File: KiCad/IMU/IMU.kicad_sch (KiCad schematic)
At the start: 10 parts, among them J1 Conn_02x20_Odd_Even

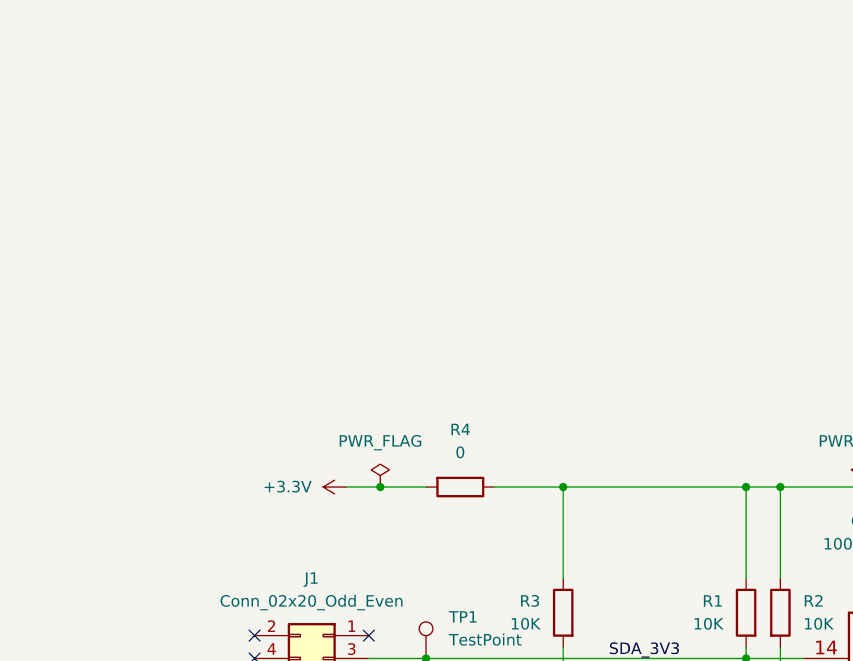
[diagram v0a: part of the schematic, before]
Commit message: Add buck 3V3 converter
Add buck 3V3 converter
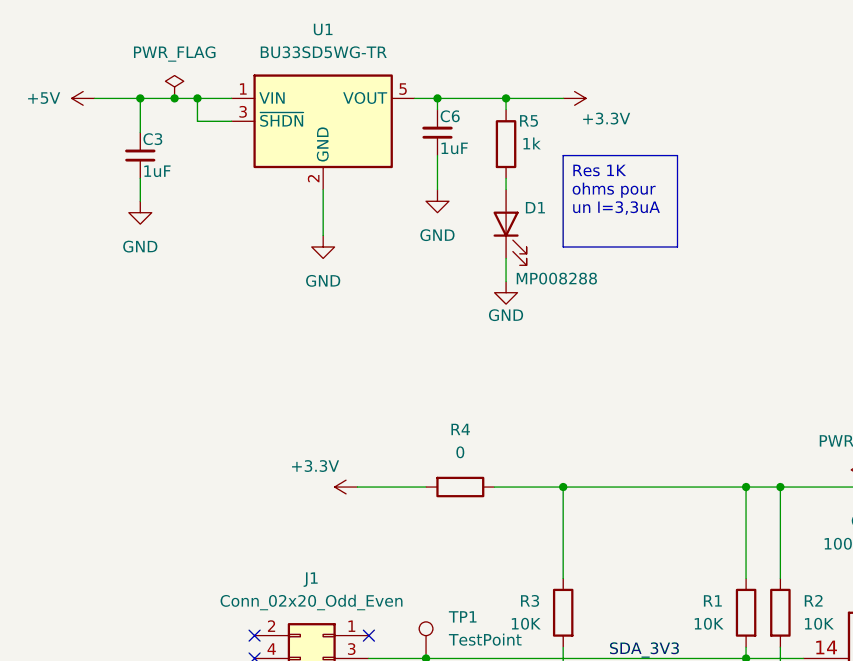
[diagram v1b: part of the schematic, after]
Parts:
- added C3, C6: 1uF, Capacitor_SMD:C_0603_1608Metric_Pad1.08x0.95mm_HandSolder, symbol Device:C_Small
- added D1: MP008288, LED_SMD:LED_0603_1608Metric, symbol Device:LED
- added R5: 1k, Resistor_SMD:R_0603_1608Metric_Pad0.98x0.95mm_HandSolder, symbol Device:R
- added U1: BU33SD5WG-TR, Package_TO_SOT_SMD:SOT-23-5, symbol Regulator_Linear:MCP1802x-xx02xOT
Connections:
- net +3.3V: now also C6.2, R5.1, U1.5 (VOUT)
- net GND: now also C3.1, C6.1, D1.1 (K), U1.2 (GND)
- new net: D1.2 (A), R5.2
- new net +5V: C3.2, U1.1 (VIN), U1.3 (~{SHDN})

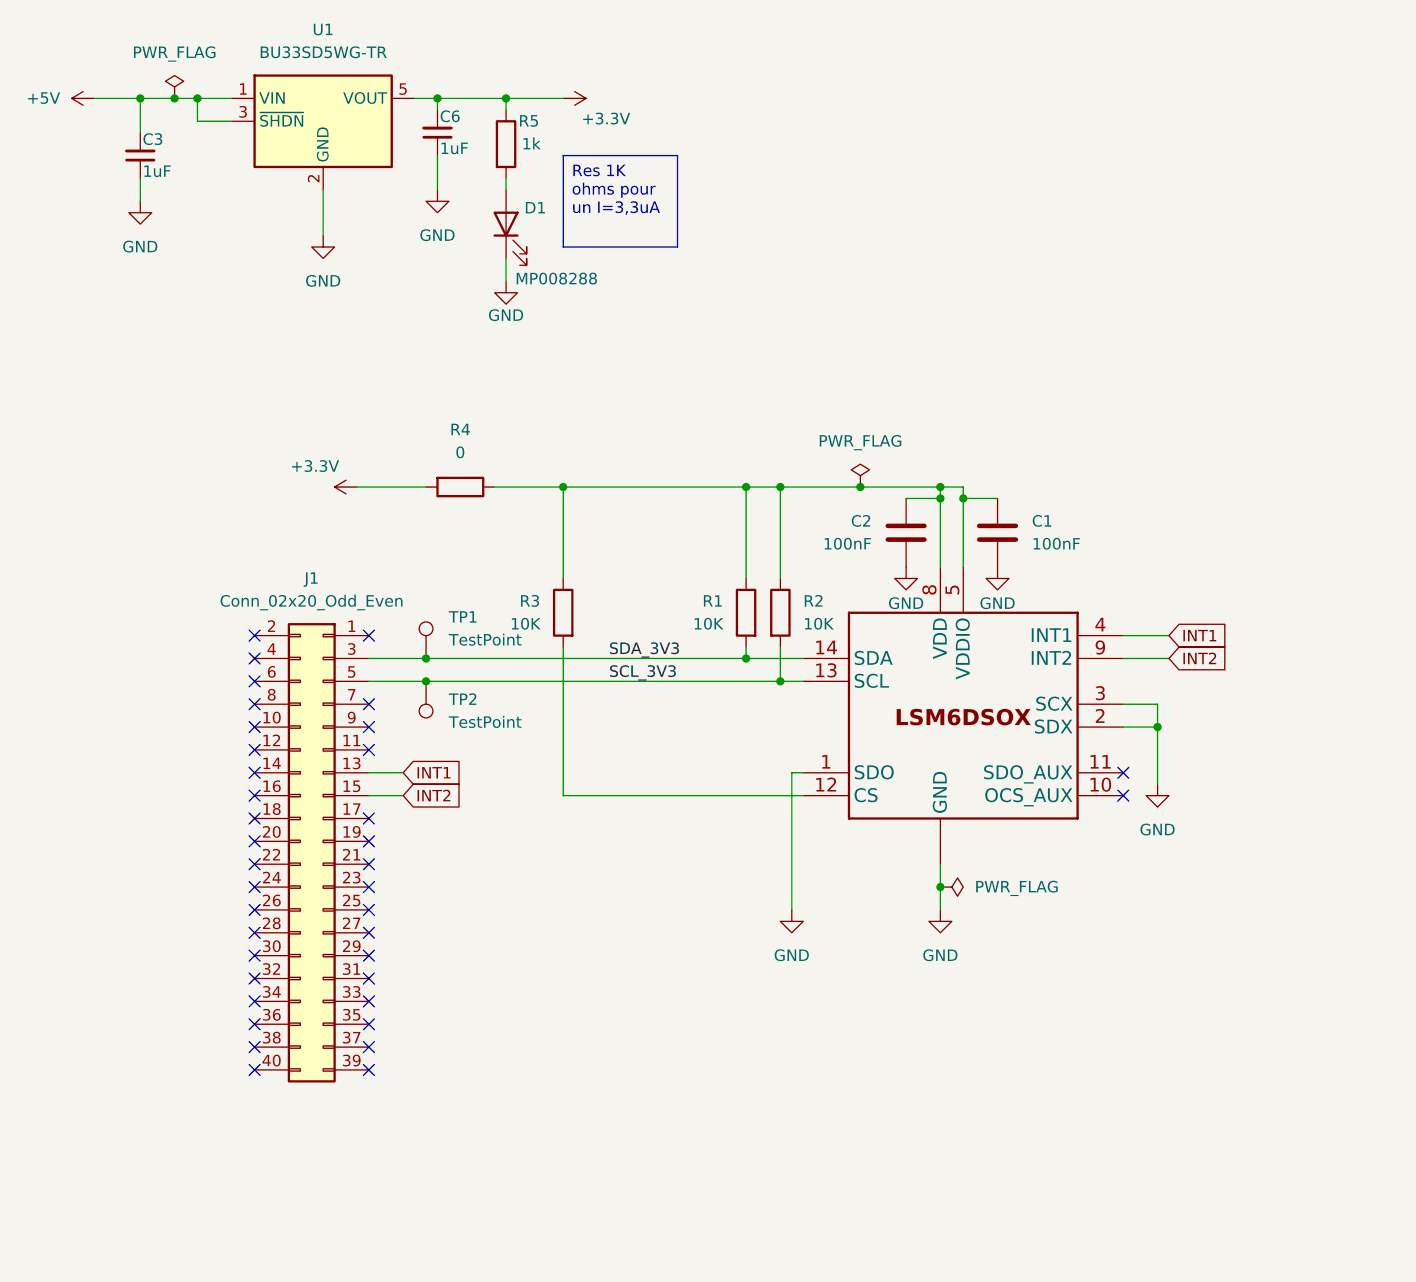
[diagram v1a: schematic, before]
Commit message: update schema IMU
remove buck converter
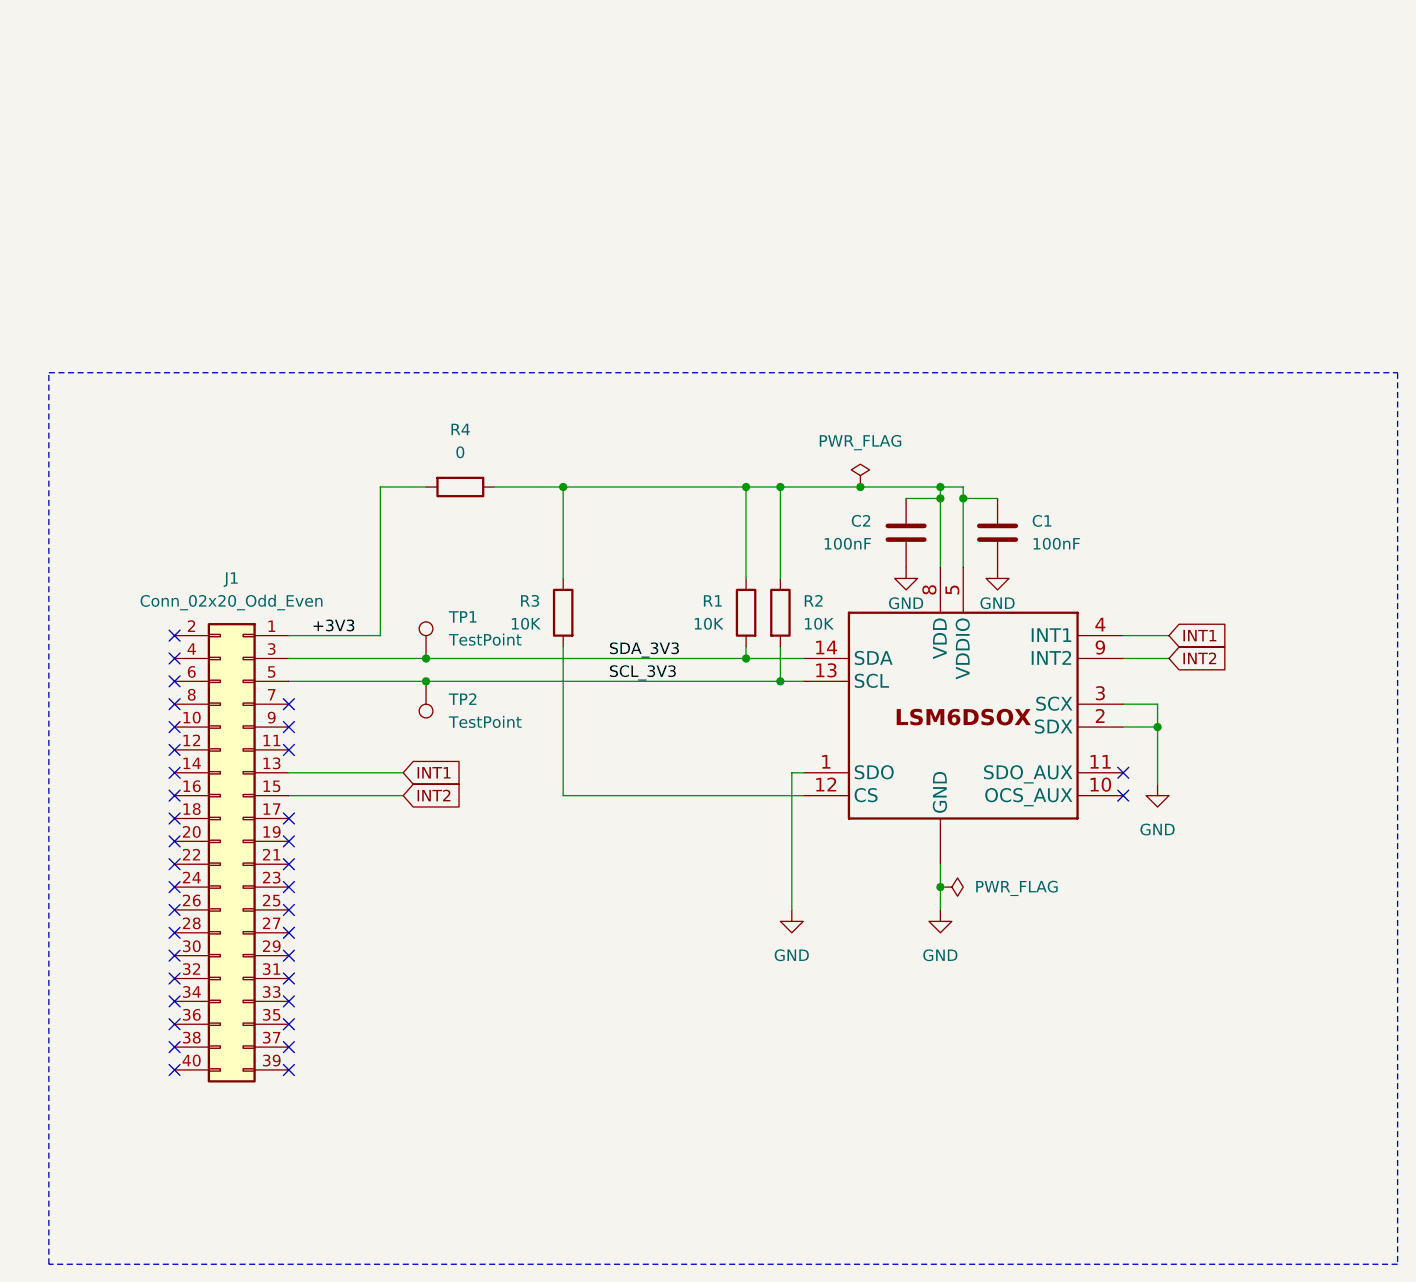
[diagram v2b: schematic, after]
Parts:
- removed C3, C6: 1uF, Capacitor_SMD:C_0603_1608Metric_Pad1.08x0.95mm_HandSolder, symbol Device:C_Small
- removed D1: MP008288, LED_SMD:LED_0603_1608Metric, symbol Device:LED
- removed R5: 1k, Resistor_SMD:R_0603_1608Metric_Pad0.98x0.95mm_HandSolder, symbol Device:R
- removed U1: BU33SD5WG-TR, Package_TO_SOT_SMD:SOT-23-5, symbol Regulator_Linear:MCP1802x-xx02xOT
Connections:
- net +3.3V is gone; now on net +3V3: R4.2
- net +3V3: now reaches J1.1 (Pin_1)
- no-connect marks 38 -> 37
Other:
- moved on the sheet: J1
